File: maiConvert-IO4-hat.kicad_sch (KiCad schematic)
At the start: 70 parts, among them J1 CN3 - From IO4, J10 1P B7, J11 1P B8, J12 2P B1, J13 2P B2, J14 2P B3, J15 2P B4, J16 2P B5, J17 2P B6, J18 2P B7, J19 2P B8, J2 CN9 - From IO4, J20 1P SELECT BUTTON, J21 2P SELECT BUTTON, J22 12V input, J23 BILLBOARD LED L, J24 BILLBOARD LED R, J25 1P CODE READER LED, J26 2P CODE READER LED, J27 COIN METER, J28 COIN LOCKOUT, J29 CAMERA LED RED, J3 CN3 - To Harness, J30 CAMERA LED WARM, J31 TEST BUTTON, J32 COIN BUTTON, J33 SERVICE BUTTON, J4 1P B1, J5 1P B2, J6 1P B3, J7 1P B4, J8 1P B5, J9 1P B6, SW1 TEST, SW10 SW_Push_Open, SW11 SW_Push_Open, SW12 SW_Push_Open, SW13 SW_Push_Open, SW14 SW_Push_Open, SW15 SW_Push_Open, SW16 SW_Push_Open, SW17 SW_Push_Open, SW18 SW_Push_Open, SW19 SW_Push_Open, SW2 COIN, SW20 SW_Push_Open, SW21 SW_Push_Open, SW3 SERVICE, SW4 1P SELECT BTN, SW5 2P SELECT BTN, SW6 SW_Push_Open, SW7 SW_Push_Open, SW8 SW_Push_Open, SW9 SW_Push_Open

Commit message: Update PCB for new components
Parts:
- D1, D2, D21, D22: footprint FabricationParts:LED_RGB_PLCC6_5050_XL5050RGBC -> LED_RGB_Wurth:LED_RGB_Wurth_WL-SFTW_150352M173300; symbol XL-5050RGBC:XL-5050RGBC -> LED_RGB_Wurth:150352M173300; Digi-Key (none) -> 732-11999-1-ND; LCSC C2843868 -> (none); Manufacturer (none) -> Wurth Elektronik; Mfr. No. (none) -> 150352M173300
- R22, R23, R24, R25, R26, R27, R28, R29, R30, R31, R32, R33: footprint Resistor_SMD:R_1206_3216Metric -> Resistor_THT:R_Axial_DIN0207_L6.3mm_D2.5mm_P10.16mm_Horizontal; Digi-Key (none) -> 1.00KXBK-ND; Manufacturer (none) -> YAGEO; Mfr. No. (none) -> MFR-25FBF52-1K
- SW1, SW2, SW3, SW4, SW5: Digi-Key (none) -> SW400-ND; Manufacturer (none) -> Omron; Mfr. No. (none) -> B3F-1000
- SW10, SW11, SW12, SW13, SW14, SW15, SW16, SW17, SW18, SW19, SW20, SW21, SW6, SW7, SW8, SW9: footprint Button_Switch_THT:SW_PUSH_6mm -> SameSky_Switch:SW_Tactile_SameSky_TS10; Digi-Key (none) -> 2223-TS10-63-26-BE-250-SMT-TRCT-ND; Manufacturer (none) -> Same Sky; Mfr. No. (none) -> TS10-63-26-BE-250-SMT-TR
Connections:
- net +12V: now also D1.2 (B+), D2.2 (B+), D21.2 (B+), D22.2 (B+); no longer D1.5 (R+), D2.5 (R+), D21.5 (R+), D22.5 (R+)
- net at R32.2: now also D22.3 (R-); no longer D22.2 (R-)
- net at R33.2: now also D22.5 (G-); no longer D22.3 (G-)
- net at R26.2: now also D2.3 (R-); no longer D2.2 (R-)
- net at R30.2: now also D21.5 (G-); no longer D21.3 (G-)
- net at R24.2: now also D1.5 (G-); no longer D1.3 (G-)
- net at R29.2: now also D21.3 (R-); no longer D21.2 (R-)
- net at R23.2: now also D1.3 (R-); no longer D1.2 (R-)
- net at R27.2: now also D2.5 (G-); no longer D2.3 (G-)

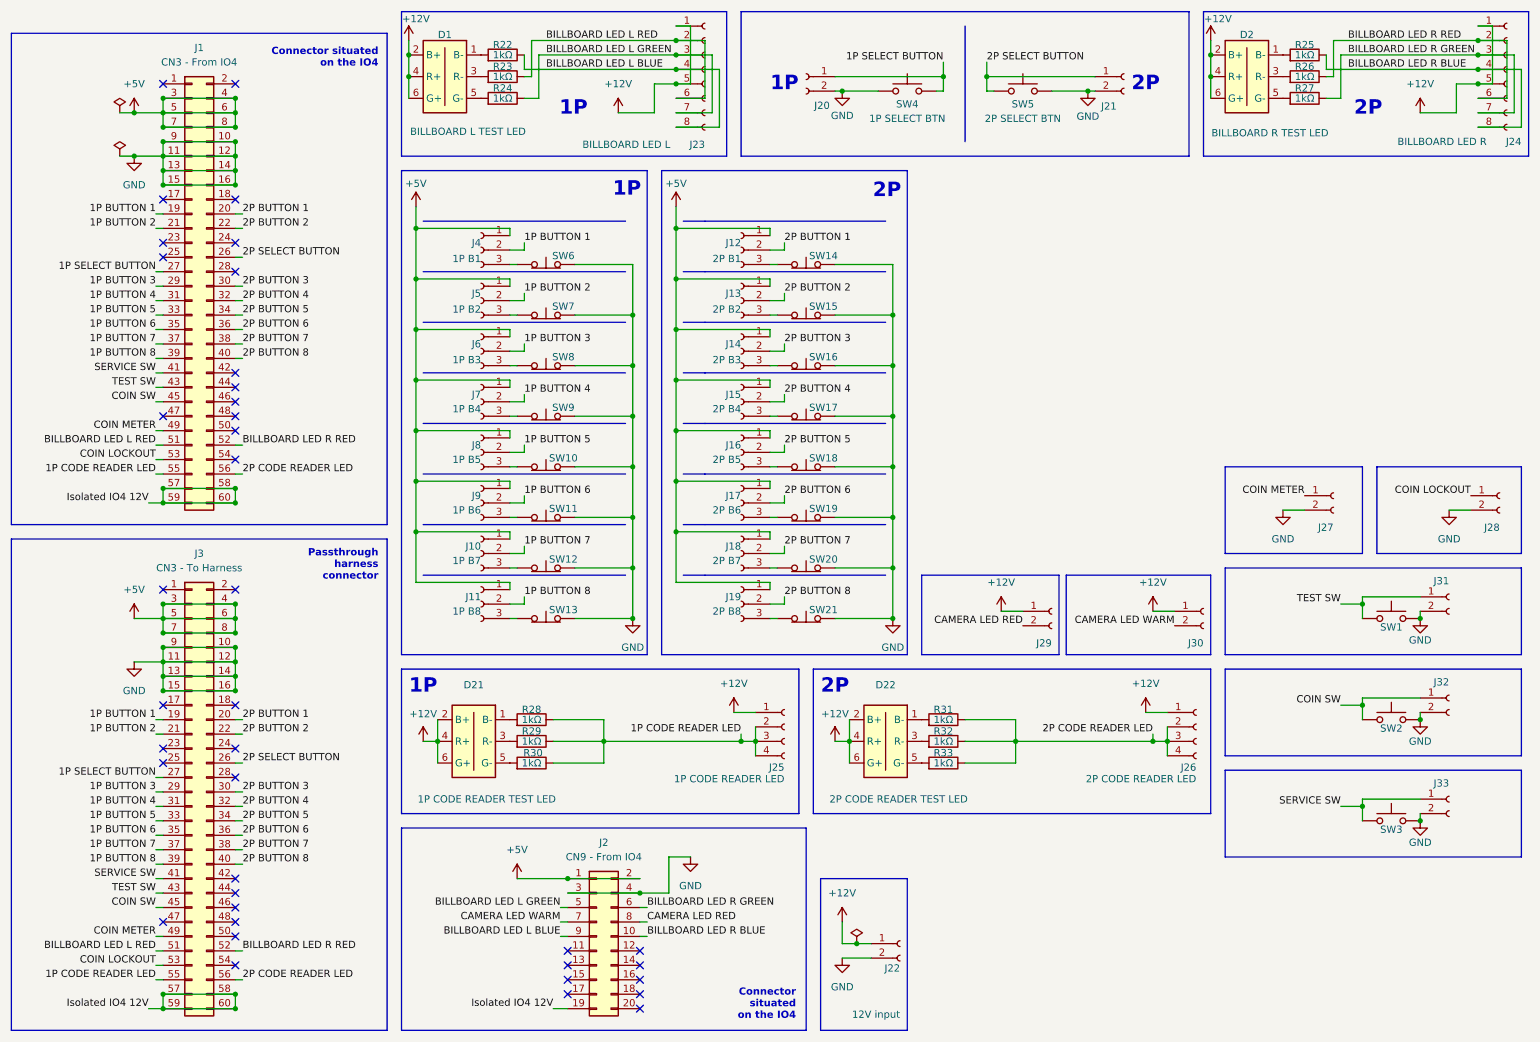
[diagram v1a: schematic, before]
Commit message: Finish mapping PCB
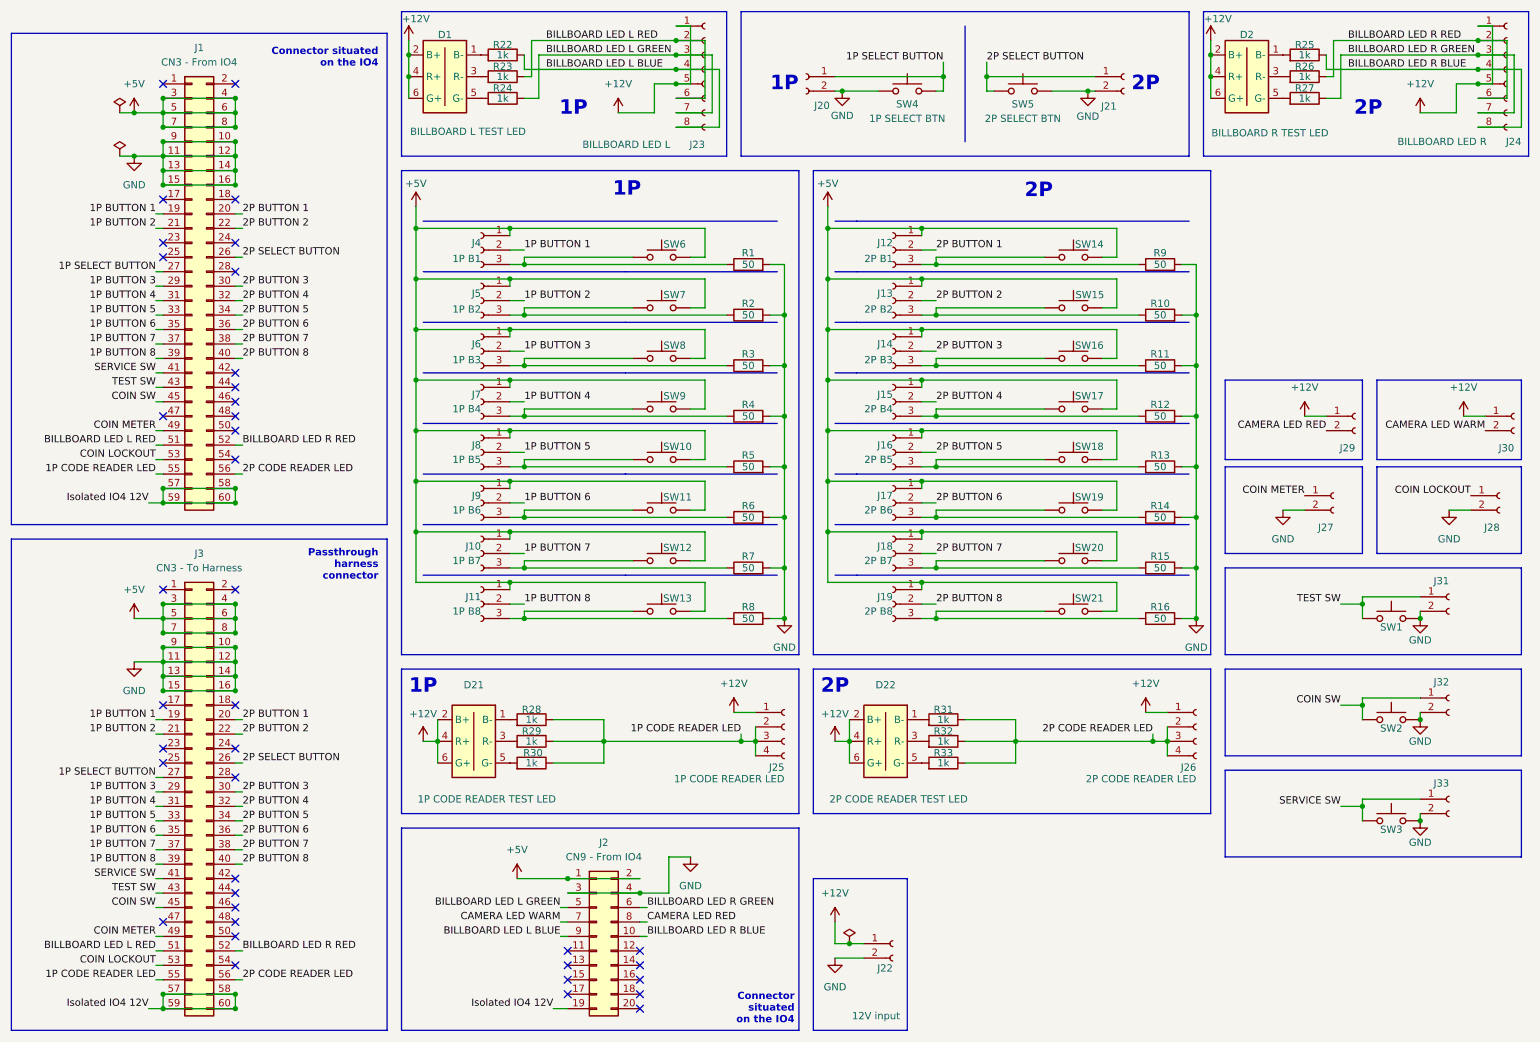
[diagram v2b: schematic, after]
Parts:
- removed SW10, SW11, SW12, SW13, SW14, SW15, SW16, SW17, SW18, SW19, SW20, SW21, SW6, SW7, SW8, SW9: SW_Push_Open, SameSky_Switch:SW_Tactile_SameSky_TS10, symbol Switch:SW_Push_Open
- added R1, R10, R11, R12, R13, R14, R15, R16, R2, R3, R4, R5, R6, R7, R8, R9: 50, Resistor_SMD:R_2512_6332Metric_Pad1.40x3.35mm_HandSolder, symbol Device:R
- added SW10: 1P B5 BTN, Button_Switch_THT:SW_PUSH_6mm, symbol Switch:SW_Push
- added SW11: 1P B6 BTN, Button_Switch_THT:SW_PUSH_6mm, symbol Switch:SW_Push
- added SW12: 1P B7 BTN, Button_Switch_THT:SW_PUSH_6mm, symbol Switch:SW_Push
- added SW13: 1P B8 BTN, Button_Switch_THT:SW_PUSH_6mm, symbol Switch:SW_Push
- added SW14: 2P B1 BTN, Button_Switch_THT:SW_PUSH_6mm, symbol Switch:SW_Push
- added SW15: 2P B2 BTN, Button_Switch_THT:SW_PUSH_6mm, symbol Switch:SW_Push
- added SW16: 2P B3 BTN, Button_Switch_THT:SW_PUSH_6mm, symbol Switch:SW_Push
- added SW17: 2P B4 BTN, Button_Switch_THT:SW_PUSH_6mm, symbol Switch:SW_Push
- added SW18: 2P B5 BTN, Button_Switch_THT:SW_PUSH_6mm, symbol Switch:SW_Push
- added SW19: 2P B6 BTN, Button_Switch_THT:SW_PUSH_6mm, symbol Switch:SW_Push
- added SW20: 2P B7 BTN, Button_Switch_THT:SW_PUSH_6mm, symbol Switch:SW_Push
- added SW21: 2P B8 BTN, Button_Switch_THT:SW_PUSH_6mm, symbol Switch:SW_Push
- added SW6: 1P B1 BTN, Button_Switch_THT:SW_PUSH_6mm, symbol Switch:SW_Push
- added SW7: 1P B2 BTN, Button_Switch_THT:SW_PUSH_6mm, symbol Switch:SW_Push
- added SW8: 1P B3 BTN, Button_Switch_THT:SW_PUSH_6mm, symbol Switch:SW_Push
- added SW9: 1P B4 BTN, Button_Switch_THT:SW_PUSH_6mm, symbol Switch:SW_Push
- J1, J3: Digi-Key (none) -> 2057-BHR-60-VUA-ND; Manufacturer (none) -> Adam Tech; Mfr. No. (none) -> BHR-60-VUA
- J10, J11, J12, J13, J14, J15, J16, J17, J18, J19, J4, J5, J6, J7, J8, J9: Digi-Key (none) -> 455-2248-ND; Manufacturer (none) -> JST; Mfr. No. (none) -> B3B-XH-A(LF)(SN)
- J2: Digi-Key (none) -> 2057-BHR-20-VUA-ND; Manufacturer (none) -> Adam Tech; Mfr. No. (none) -> BHR-20-VUA
- J20, J21, J27, J28, J29, J30, J31, J32, J33: Digi-Key (none) -> 455-2247-ND; Manufacturer (none) -> JST; Mfr. No. (none) -> B2B-XH-A(LF)(SN)
- J22: Digi-Key (none) -> 277-1667-ND; Manufacturer (none) -> Phoenix Contact; Mfr. No. (none) -> 1935161
- J23, J24: Digi-Key (none) -> 455-B8B-XH-A-ND; Manufacturer (none) -> JST; Mfr. No. (none) -> B8B-XH-A(LF)(SN)
- J25, J26: Digi-Key (none) -> 455-2249-ND; Manufacturer (none) -> JST; Mfr. No. (none) -> B4B-XH-A(LF)(SN)
- R22, R23, R24, R25, R26, R27, R28, R29, R30, R31, R32, R33: value 1kΩ -> 1k; footprint Resistor_THT:R_Axial_DIN0207_L6.3mm_D2.5mm_P10.16mm_Horizontal -> Resistor_SMD:R_1206_3216Metric_Pad1.30x1.75mm_HandSolder; Digi-Key 1.00KXBK-ND -> 311-1.00KFRCT-ND; Mfr. No. MFR-25FBF52-1K -> RC1206FR-071KL
- SW1, SW2, SW3, SW4, SW5: Digi-Key SW400-ND -> 2223-TS02-66-60-BK-100-LCR-D-ND; Manufacturer Omron -> Same Sky; Mfr. No. B3F-1000 -> TS02-66-60-BK-100-LCR-D
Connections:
- net +5V: now also SW10.2, SW11.2, SW12.2, SW13.2, SW14.2, SW15.2, SW16.2, SW17.2, SW18.2, SW19.2, SW20.2, SW21.2, SW6.2, SW7.2, SW8.2, SW9.2
- net 1P SELECT BUTTON: now also SW4.1; no longer SW4.2
- net GND: now also SW4.2, R1.2, R10.2, R11.2, R12.2, R13.2, R14.2, R15.2, R16.2, R2.2, R3.2, R4.2, R5.2, R6.2, R7.2, R8.2, R9.2; no longer SW4.1
- net at J17.3 (Pin_3): now also R14.1, SW19.1
- net at J8.3 (Pin_3): now also R5.1, SW10.1
- net at J19.3 (Pin_3): now also R16.1, SW21.1
- net at J7.3 (Pin_3): now also R4.1, SW9.1
- net at J4.3 (Pin_3): now also R1.1, SW6.1
- net at J10.3 (Pin_3): now also R7.1, SW12.1
- net at J9.3 (Pin_3): now also R6.1, SW11.1
- net at J15.3 (Pin_3): now also R12.1, SW17.1
- net at J5.3 (Pin_3): now also R2.1, SW7.1
- net at J6.3 (Pin_3): now also R3.1, SW8.1
- net at J16.3 (Pin_3): now also R13.1, SW18.1
- net at J12.3 (Pin_3): now also R9.1, SW14.1
- net at J13.3 (Pin_3): now also R10.1, SW15.1
- net at J11.3 (Pin_3): now also R8.1, SW13.1
- net at J14.3 (Pin_3): now also R11.1, SW16.1
- net at J18.3 (Pin_3): now also R15.1, SW20.1
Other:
- moved on the sheet: J12, J13, J14, J15, J16, J17, J18, J19, J22, J29, J30
